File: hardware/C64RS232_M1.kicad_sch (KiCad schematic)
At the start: 9 parts, among them J1 C64 USER PORT, J2 5747844-4, U1 MAX3243EIPWR

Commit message: Generate M1.10 KiCad schematic baseline
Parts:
- J2: footprint Connector_Dsub:DSUB-9_Female_Horizontal_P2.77x2.84mm_EdgePinOffset9.40mm_Housed_MountingHolesOffset11.32mm -> C64RS232:TE_5747844-4

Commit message: Correct C64 User Port RS-232 signal mapping
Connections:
- net C64_CTS: no longer J1.K (PB6)
- net C64_DCD: now also J1.E (PB2); no longer J1.H (PB4)
- net C64_DSR: now also J1.B (FLAG2); no longer J1.L (PB7)
- net C64_DTR: now also J1.H (PB4); no longer J1.E (PB2)
- net C64_RTS: no longer J1.D (PB1)
- net C64_RXD: now also J1.K (PB6); no longer J1.B (FLAG2)
- net C64_TXD: now also J1.A (GND); no longer J1.M (PA2)
- net GND: now also J1.M (PA2); no longer J1.1 (GND), J1.A (GND)
- net RAW_5V: no longer J1.2 (+5V)
- new net C64_UNUSED_J: J1.D (PB1)
- new net FLAG2: J1.L (PB7)
- new net NO_CONNECT_9VAC+: J1.2 (+5V)
- new net NO_CONNECT_9VAC-: J1.1 (GND)
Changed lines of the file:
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@@
 		)
 	)
-	(label "C64_TXD"
+	(label "GND"
 		(at 33.02 109.22 0)
 		(effects
@@
 		)
 	)
-	(label "GND"
+	(label "NO_CONNECT_9VAC-"
 		(at 58.42 83.82 0)
 		(effects
@@
 		)
 	)
-	(label "C64_RXD"
+	(label "C64_DSR"
 		(at 33.02 86.36 0)
 		(effects
@@
 		)
 	)
+	(label "C64_DCD"
+		(at 33.02 93.98 0)
+		(effects
+			(font
+				(size 1.27 1.27)
+			)
+			(justify left bottom)
+		)
+	)
 	(label "C64_DTR"
-		(at 33.02 93.98 0)
-		(effects
-			(font
-				(size 1.27 1.27)
-			)
-			(justify left bottom)
-		)
-	)
-	(label "C64_DCD"
 		(at 33.02 99.06 0)
 		(effects
@@
 		)
 	)
-	(label "C64_CTS"
+	(label "C64_RXD"
 		(at 33.02 104.14 0)
 		(effects
@@
 		)
 	)
-	(label "GND"
+	(label "C64_TXD"
 		(at 33.02 83.82 0)
 		(effects
@@
 		)
 	)
-	(label "RAW_5V"
+	(label "NO_CONNECT_9VAC+"
 		(at 58.42 86.36 0)
 		(effects
@@
 		)
 	)
-	(label "C64_RTS"
+	(label "C64_UNUSED_J"
 		(at 33.02 91.44 0)
 		(effects
@@
 		)
 	)
-	(label "C64_DSR"
+	(label "FLAG2"
 		(at 33.02 106.68 0)
 		(effects

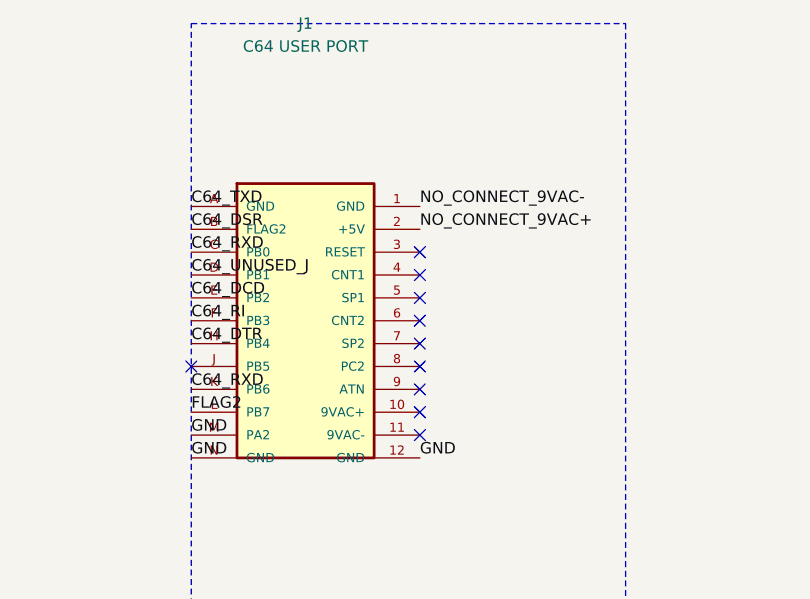
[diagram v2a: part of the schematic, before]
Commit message: Complete and sanitize C64 User Port pin mapping
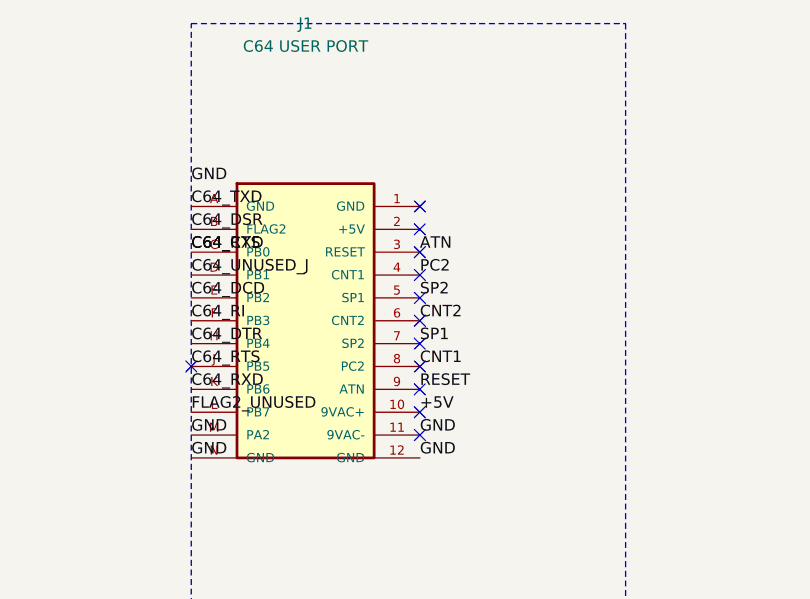
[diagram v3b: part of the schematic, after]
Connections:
- net C64_RXD is gone; now on net C64_CTS: J1.C (PB0), J1.K (PB6), U1.19 (R1OUT)
- net +5V: now also J1.10 (9VAC+)
- net C64_RTS: now also J1.J (PB5)
- net GND: now also J1.11 (9VAC-)
- net ATN: now reaches J1.3 (RESET)
- net PC2: now reaches J1.4 (CNT1)
- net SP2: now reaches J1.5 (SP1)
- net CNT2: now reaches J1.6 (CNT2)
- net SP1: now reaches J1.7 (SP2)
- net CNT1: now reaches J1.8 (PC2)
- net RESET: now reaches J1.9 (ATN)
- net FLAG2 renamed FLAG2_UNUSED
- net NO_CONNECT_9VAC+: no longer names the net of J1.2 (+5V)
- net NO_CONNECT_9VAC-: no longer names the net of J1.1 (GND)
- no-connect marks 12 -> 14
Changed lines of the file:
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@@
 	(label "GND"
 		(at 33.02 109.22 0)
-		(effects
-			(font
-				(size 1.27 1.27)
-			)
-			(justify left bottom)
-		)
-	)
-	(label "NO_CONNECT_9VAC-"
-		(at 58.42 83.82 0)
-		(effects
-			(font
-				(size 1.27 1.27)
-			)
-			(justify left bottom)
-		)
-	)
+		(effects (font (size 1.27 1.27)) (justify left bottom))
+	)
+	(no_connect (at 58.42 83.82))
 	(label "GND"
 		(at 203.2 96.52 0)
@@
 	(label "C64_RI"
 		(at 33.02 96.52 0)
-		(effects
-			(font
-				(size 1.27 1.27)
-			)
-			(justify left bottom)
-		)
+		(effects (font (size 1.27 1.27)) (justify left bottom))
 	)
 	(label "RS232_TXD"
@@
 	(label "C64_DSR"
 		(at 33.02 86.36 0)
-		(effects
-			(font
-				(size 1.27 1.27)
-			)
-			(justify left bottom)
-		)
+		(effects (font (size 1.27 1.27)) (justify left bottom))
 	)
 	(label "GND"
@@
 	(label "C64_DCD"
 		(at 33.02 93.98 0)
-		(effects
-			(font
-				(size 1.27 1.27)
-			)
-			(justify left bottom)
-		)
+		(effects (font (size 1.27 1.27)) (justify left bottom))
 	)
 	(label "C64_DTR"
 		(at 33.02 99.06 0)
-		(effects
-			(font
-				(size 1.27 1.27)
-			)
-			(justify left bottom)
-		)
+		(effects (font (size 1.27 1.27)) (justify left bottom))
 	)
 	(label "GND"
@@
 	(label "C64_RXD"
 		(at 33.02 104.14 0)
-		(effects
-			(font
-				(size 1.27 1.27)
-			)
-			(justify left bottom)
-		)
+		(effects (font (size 1.27 1.27)) (justify left bottom))
 	)
 	(label "RS232_RTS"
@@
 	(label "C64_TXD"
 		(at 33.02 83.82 0)
-		(effects
-			(font
-				(size 1.27 1.27)
-			)
-			(justify left bottom)
-		)
+		(effects (font (size 1.27 1.27)) (justify left bottom))
 	)
 	(label "RS232_DSR"
@@
 		)
 	)
-	(label "NO_CONNECT_9VAC+"
-		(at 58.42 86.36 0)
-		(effects
-			(font
-				(size 1.27 1.27)
-			)
-			(justify left bottom)
-		)
-	)
+	(no_connect (at 58.42 86.36))
 	(label "+5V"
 		(at 177.8 41.91 0)
@@
 	(label "C64_UNUSED_J"
 		(at 33.02 91.44 0)
-		(effects
-			(font
-				(size 1.27 1.27)
-			)
-			(justify left bottom)
-		)
+		(effects (font (size 1.27 1.27)) (justify left bottom))
 	)
 	(label "C2_MINUS"
@@
 		)
 	)
-	(label "FLAG2"
+	(label "FLAG2_UNUSED"
 		(at 33.02 106.68 0)
-		(effects
-			(font
-				(size 1.27 1.27)
-			)
-			(justify left bottom)
-		)
+		(effects (font (size 1.27 1.27)) (justify left bottom))
 	)
 	(label "RS232_RI"
@@
 		)
 	)
+(label "C64_RTS"
+		(at 33.02 101.60 0)
+		(effects (font (size 1.27 1.27)) (justify left bottom))
+	)
+(label "C64_CTS"
+		(at 33.02 88.90 0)
+		(effects (font (size 1.27 1.27)) (justify left bottom))
+	)
+(label "GND"
+		(at 33.02 81.28 0)
+		(effects (font (size 1.27 1.27)) (justify left bottom))
+	)
+(label "GND"
+		(at 58.42 109.22 0)
+		(effects (font (size 1.27 1.27)) (justify left bottom))
+	)
+(label "+5V"
+		(at 58.42 106.68 0)
+		(effects (font (size 1.27 1.27)) (justify left bottom))
+	)
+(label "RESET"
+		(at 58.42 104.14 0)
+		(effects (font (size 1.27 1.27)) (justify left bottom))
+	)
+(label "CNT1"
+		(at 58.42 101.60 0)
+		(effects (font (size 1.27 1.27)) (justify left bottom))
+	)
+(label "SP1"
+		(at 58.42 99.06 0)
+		(effects (font (size 1.27 1.27)) (justify left bottom))
+	)
+(label "CNT2"
+		(at 58.42 96.52 0)
+		(effects (font (size 1.27 1.27)) (justify left bottom))
+	)
+(label "SP2"
+		(at 58.42 93.98 0)
+		(effects (font (size 1.27 1.27)) (justify left bottom))
+	)
+(label "PC2"
+		(at 58.42 91.44 0)
+		(effects (font (size 1.27 1.27)) (justify left bottom))
+	)
+(label "ATN"
+		(at 58.42 88.90 0)
+		(effects (font (size 1.27 1.27)) (justify left bottom))
+	)
 	(sheet_instances
